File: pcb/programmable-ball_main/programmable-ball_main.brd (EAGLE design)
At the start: 30 x 30 mm, 34 parts, among them J1 12402012E212A, J3 B4B-ZR-SM4-TFT(LF)(SN), P1 S2B-ZR-SM4A-TF, Q1 DMG2305UX-13, U1 MDBT50Q-1MV2, U2 AP2112K-3.3TRG1, U3 MCP73832T-2ACI/OT, Y1 FC-135_32.7680KA-A0

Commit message: v2の軽微な修正
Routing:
- net GND: track 116.6 -> 117.5 mm
- added copper zone on layer 1, net GND

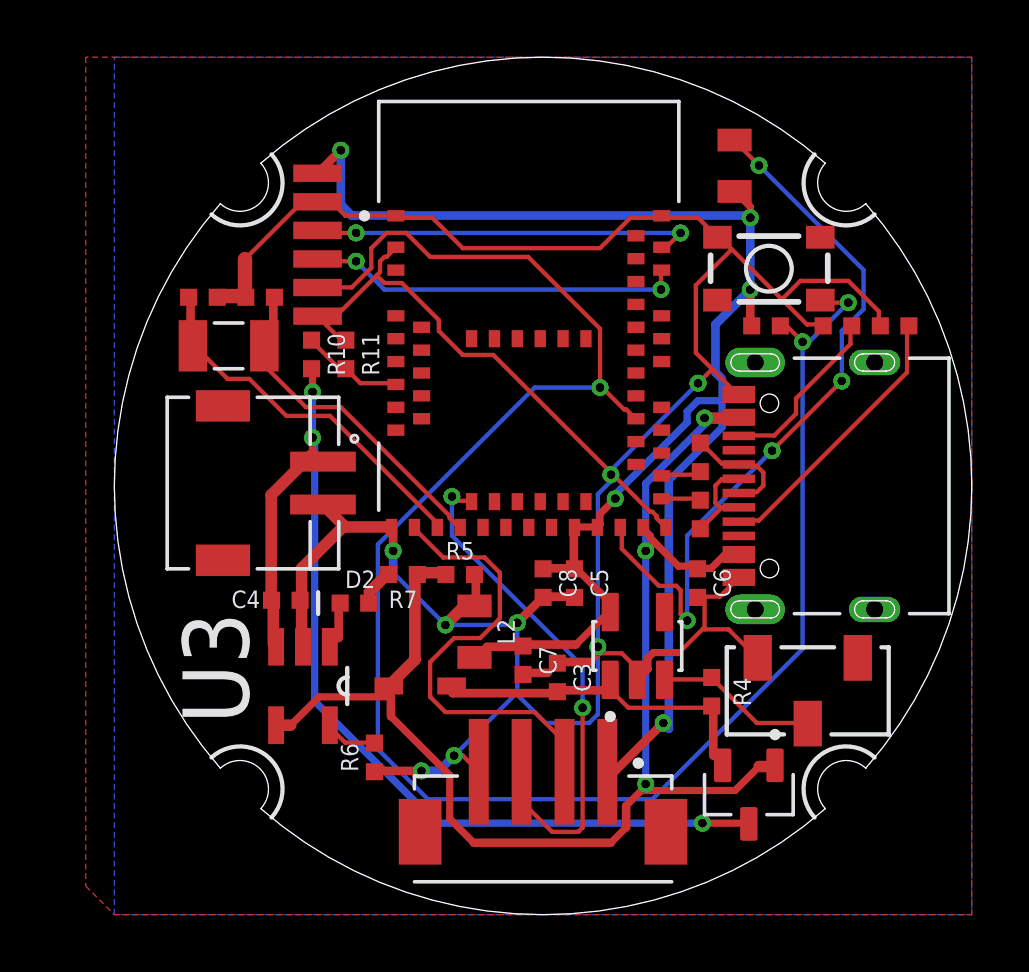
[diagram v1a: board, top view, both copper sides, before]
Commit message: シルクの削除
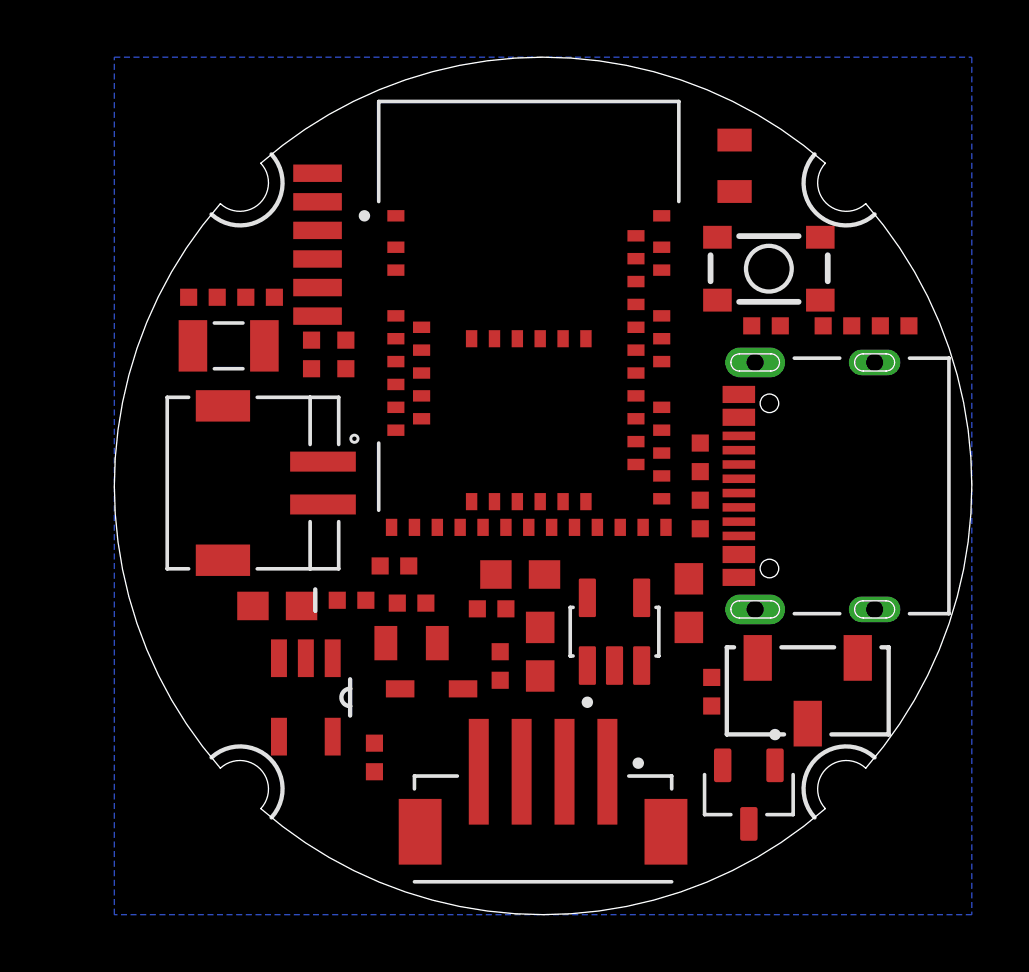
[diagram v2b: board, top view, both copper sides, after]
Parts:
- C3, C4, C5, C6: device SparkFun-Capacitors:0402-TIGHT -> SparkFun-Capacitors:0603
- moved L2 2.24 mm to (10.4, 9.50), turned to 180 degrees
- moved C8 2.01 mm to (13.2, 10.7), turned to 180 degrees
- moved R5 1.97 mm to (10.4, 10.9), turned to 0 degrees
- moved C5 1.92 mm to (14.2, 11.9), turned to 180 degrees
- moved C3 1.08 mm to (14.9, 9.20), turned to 90 degrees
- moved U2 0.94 mm to (17.5, 9.90)
- moved C7 0.82 mm to (13.5, 8.70)
- moved C6 0.76 mm to (20.1, 10.9)
- moved R7 0.42 mm to (9.80, 12.2)
- moved U3 0.41 mm to (6.70, 7.60)
- moved D1 0.41 mm to (11.1, 7.90)
- moved C4 0.36 mm to (5.70, 10.8), turned to 0 degrees
- moved D2 0.14 mm to (8.30, 11.0)
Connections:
- net GND: now also C3.2, C4.2; no longer C3.1, C4.1
- net N$6: now also C3.1; no longer C3.2
- net VBAT: now also C4.1; no longer C4.2
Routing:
- net GND: track 117.5 -> 0.00 mm, vias 8 -> 0
- net RESET: track 66.1 -> 0.00 mm, vias 3 -> 0
- net 3.3V: track 59.8 -> 0.00 mm, vias 5 -> 0
- net VBUS: track 48.4 -> 0.00 mm, vias 3 -> 0
- net VBAT: track 37.5 -> 0.00 mm, vias 3 -> 0
- net N$5: track 25.8 -> 0.00 mm, vias 4 -> 0
- net I2C_SDA: track 17.9 -> 0.00 mm, vias 2 -> 0
- net I2C_SCL: track 16.0 -> 0.00 mm
- net SWDCLK: track 13.6 -> 0.00 mm, vias 2 -> 0
- net SWDIO: track 13.1 -> 0.00 mm, vias 2 -> 0
- net N$4: track 13.0 -> 0.00 mm
- net N$6: track 12.5 -> 0.00 mm
- net N$3: track 11.8 -> 0.00 mm
- net N$1: track 9.73 -> 0.00 mm
- net N$2: track 6.21 -> 0.00 mm
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- removed copper zone on layer 1, net GND

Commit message: 最新版に変更
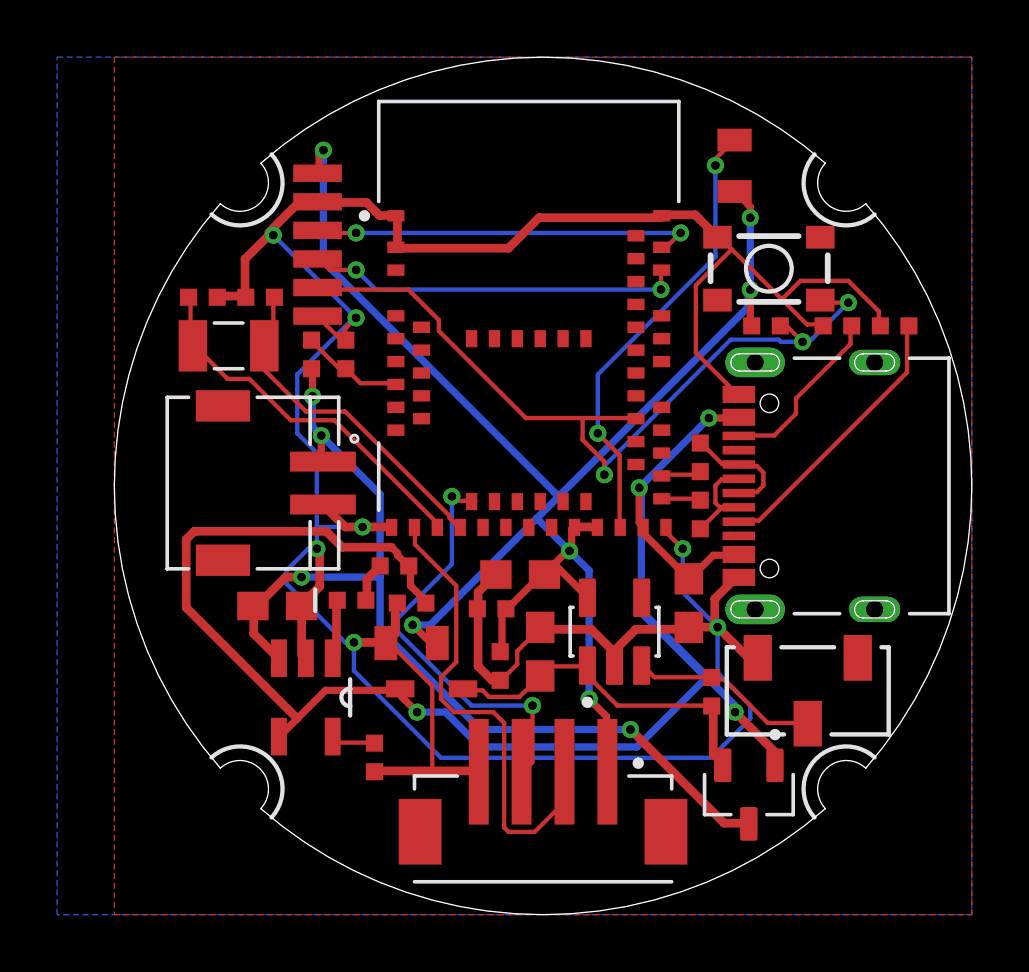
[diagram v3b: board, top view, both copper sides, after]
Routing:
- net GND: track 0.00 -> 122.4 mm, vias 0 -> 7
- net 3.3V: track 0.00 -> 57.8 mm, vias 0 -> 6
- net VBUS: track 0.00 -> 57.7 mm, vias 0 -> 4
- net VBAT: track 0.00 -> 33.8 mm, vias 0 -> 4
- net RESET: track 0.00 -> 28.9 mm, vias 0 -> 3
- net I2C_SCL: track 0.00 -> 16.7 mm
- net N$5: track 0.00 -> 15.9 mm, vias 0 -> 2
- net I2C_SDA: track 0.00 -> 14.6 mm, vias 0 -> 2
- net SWDCLK: track 0.00 -> 13.6 mm, vias 0 -> 2
- net SWDIO: track 0.00 -> 13.1 mm, vias 0 -> 2
- net N$4: track 0.00 -> 13.0 mm
- net N$6: track 0.00 -> 12.3 mm
- net N$3: track 0.00 -> 11.9 mm
- net N$1: track 0.00 -> 9.73 mm
- net EN: track 0.00 -> 6.65 mm
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- added copper zone on layer 1, net GND
